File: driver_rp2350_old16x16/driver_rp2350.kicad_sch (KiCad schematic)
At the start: 0 parts

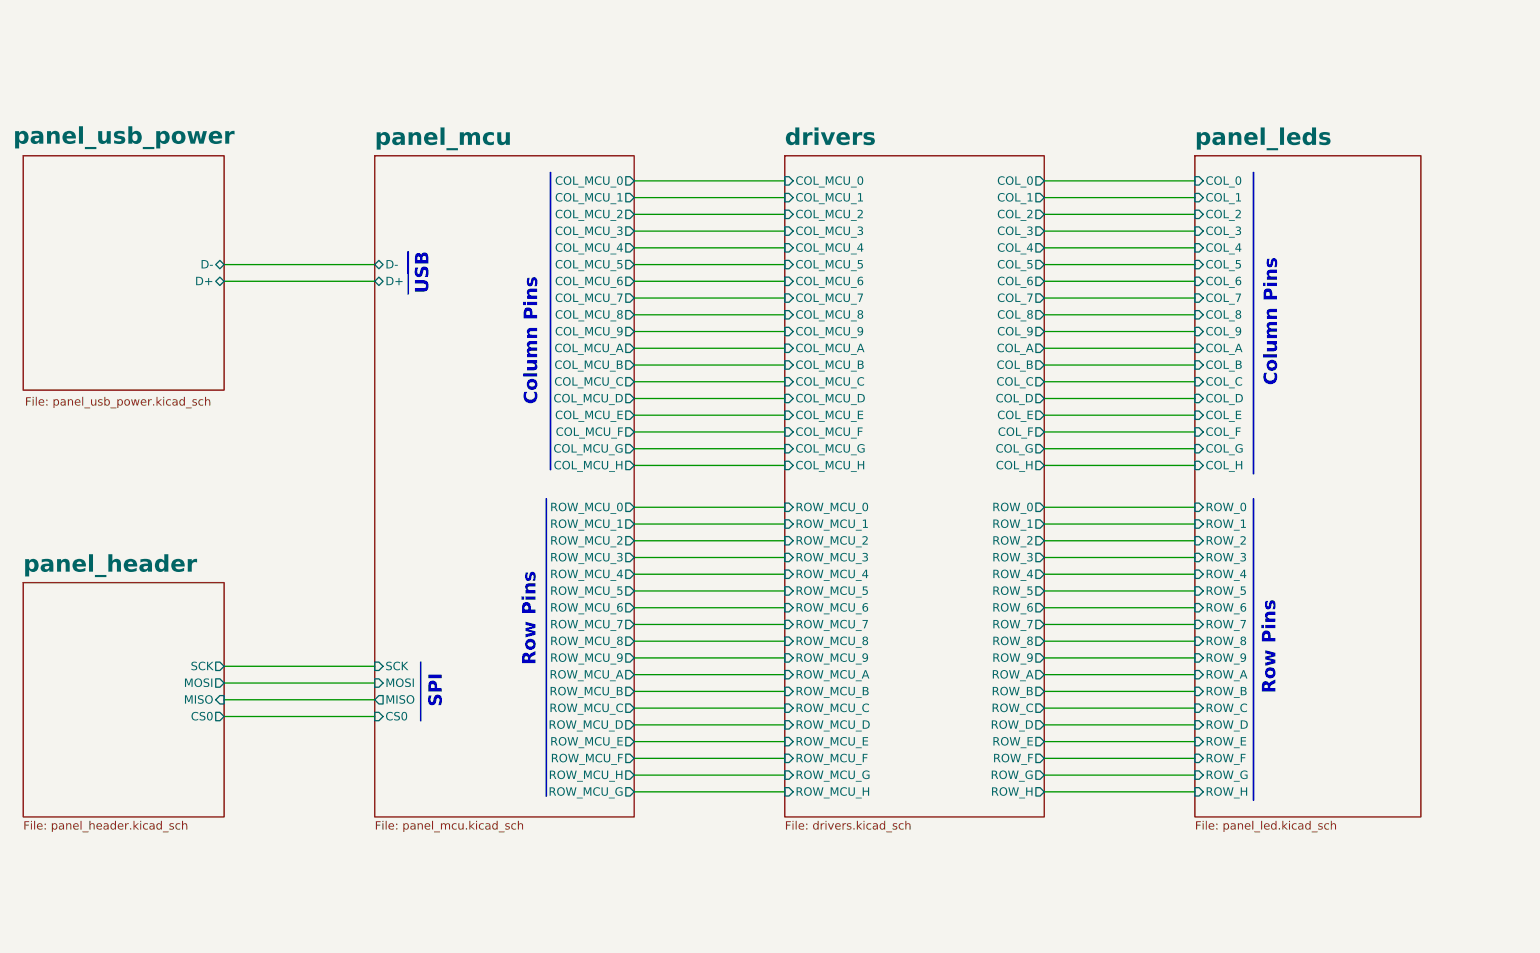
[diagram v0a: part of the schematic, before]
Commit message: Worked on new 18x18 led version of rp2350 design.
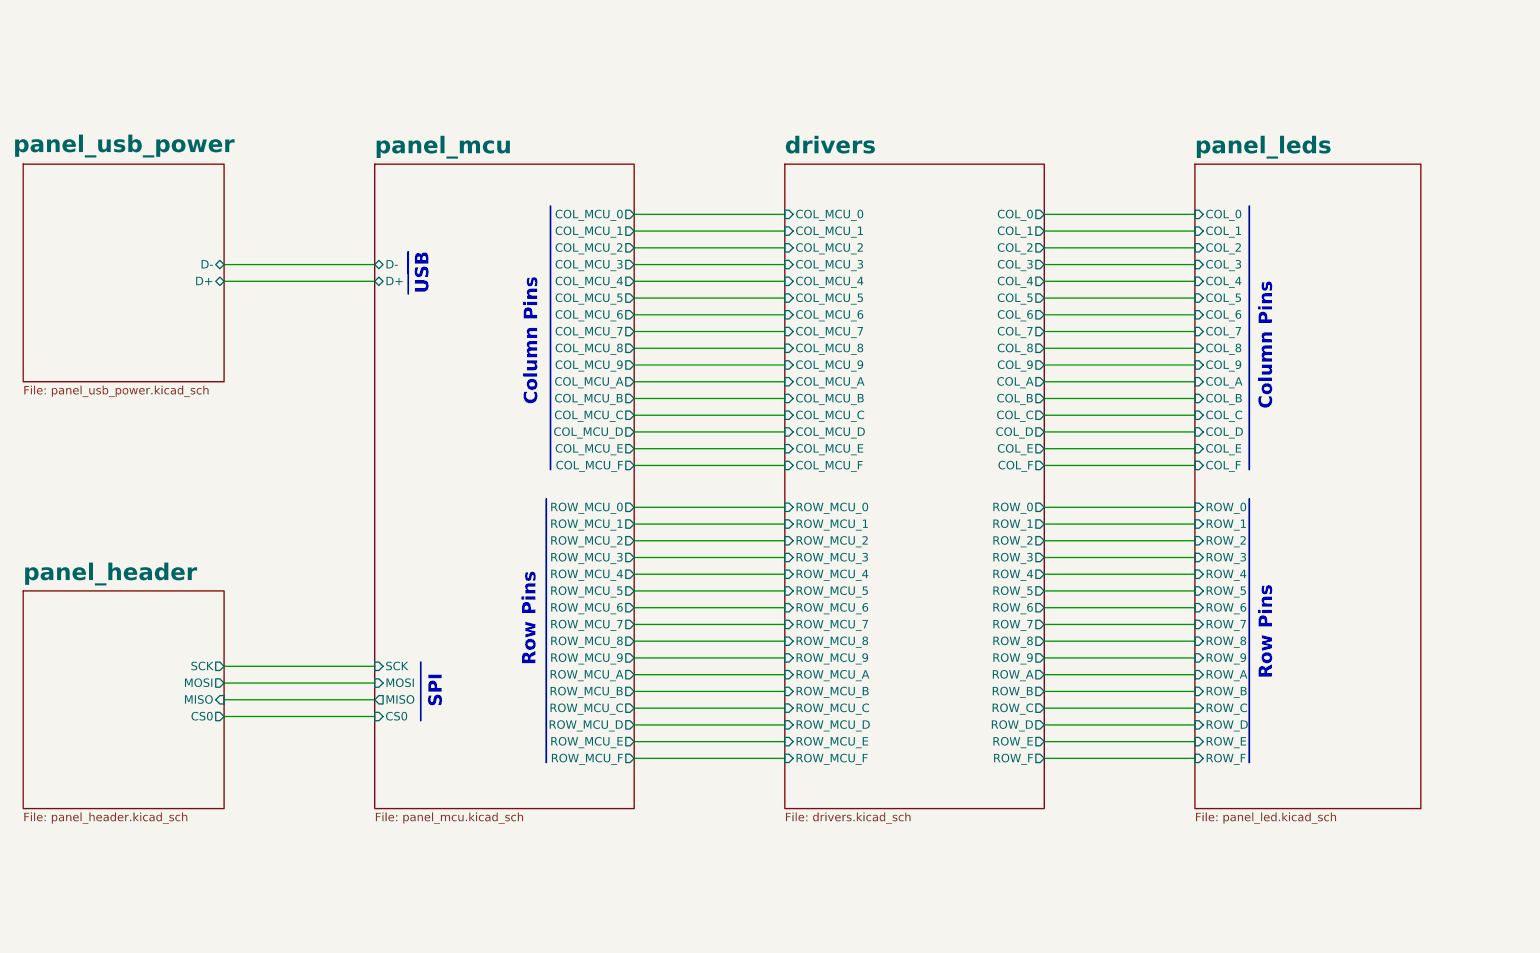
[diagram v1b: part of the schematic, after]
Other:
- sheet drivers ports: added none; removed COL_G, COL_H, COL_MCU_G, COL_MCU_H, ROW_G, ROW_H, ROW_MCU_G, ROW_MCU_H
- sheet panel_leds ports: added none; removed COL_G, COL_H, ROW_G, ROW_H
- sheet panel_mcu ports: added none; removed COL_MCU_G, COL_MCU_H, ROW_MCU_G, ROW_MCU_H
